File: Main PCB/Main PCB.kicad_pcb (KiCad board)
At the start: 2 copper layers, 100 x 70 mm, 43 parts, among them J1 Power Input, J10 Conn_01x03_Pin, J11 Conn_01x03_Pin, J12 Conn_01x03_Pin, J13 Conn_01x03_Pin, J14 Conn_01x03_Pin, J15 Conn_01x03_Pin, J16 Spare I2C PINS, J2 2nd PCB, J3 Servo Motor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

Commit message: Second revision
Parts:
- removed C4: C, Capacitor_THT:C_Disc_D3.8mm_W2.6mm_P2.50mm
- added C12: 10nF, Capacitor_THT:C_Disc_D3.8mm_W2.6mm_P2.50mm, F.Cu at (135.5, 128.0)
- added C13: 10uF, Capacitor_THT:C_Disc_D5.0mm_W2.5mm_P5.00mm, F.Cu at (152.8, 112.5)
- added J17: Trigger Pin (backup), Connector_PinHeader_2.54mm:PinHeader_1x01_P2.54mm_Vertical, F.Cu at (107.8, 108.5)
- added R7: 100, Resistor_THT:R_Axial_DIN0207_L6.3mm_D2.5mm_P10.16mm_Horizontal, F.Cu at (121.7, 138.0)
- C1: value 0.1uF -> 10nF; footprint Capacitor_THT:CP_Radial_D5.0mm_P2.50mm -> Capacitor_THT:C_Disc_D3.8mm_W2.6mm_P2.50mm
- C3: value 0.1uF -> 1uF
- J7: value GPS Module -> Conn_01x05_Pin; footprint Connector_PinSocket_2.54mm:PinSocket_1x04_P2.54mm_Vertical -> Connector_PinHeader_2.54mm:PinHeader_1x05_P2.54mm_Vertical
- R1: value 10.8k -> 11k
- R2: value 3.01k -> 3k
- R3: value 3.09k -> 3k
- U1: value ~ -> CA3140
- moved J7 48.0 mm to (115.5, 86.5), turned to 0 degrees
- moved R3 9.95 mm to (152.9, 131.5)
- moved C3 9.78 mm to (141.0, 126.5), turned to 0 degrees
- moved C1 9.14 mm to (123.0, 130.2)
- moved U1 6.25 mm to (149.3, 121.3), turned to 180 degrees
- moved TH1 5.56 mm to (131.2, 132.0)
- moved J6 4.85 mm to (148.9, 102.2)
- moved C9 4.72 mm to (160.5, 106.5)
- moved J16 4.13 mm to (148.9, 97.2)
- moved J4 3.74 mm to (107.8, 104.7)
- moved R5 3.58 mm to (156.8, 113.2)
- moved R1 3.54 mm to (136.9, 133.5), turned to 0 degrees
- moved C7 2.80 mm to (160.5, 100.5)
- moved R4 2.80 mm to (92.4, 88.2)
- moved J1 2.72 mm to (76.2, 90.2), turned to 0 degrees
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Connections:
- A1 pad 1: unconnected-(A1-D1/TX-Pad1) -> /D1/TX
- A1 pad 10: unconnected-(A1-D7-Pad10) -> /Trigger
- A1 pad 2: unconnected-(A1-D0/RX-Pad2) -> /D0/RX
- A1 pad 3: unconnected-(A1-~{RESET}-Pad3) -> /PC6/RESET
- A1 pad 5: unconnected-(A1-D2-Pad5) -> /D2
- A1 pad 7: unconnected-(A1-D4-Pad7) -> /D4
- C1 pad 1: +5V -> GND
- C1 pad 2: GND -> +5V
- J7 pad 1: +5V -> /D1/TX
- J7 pad 2: GND -> /D0/RX
- J7 pad 3: /SDA -> /PC6/RESET
- J7 pad 4: /SCL -> /D2
- R2 pad 1: +5V -> Net-(R2-Pad1)
- U1 pad 1: Net-(U1-+) -> unconnected-(U1-NULL-Pad1)
- U1 pad 3: +5V -> Net-(U1-+)
- U1 pad 5: /NTC_Vout(ADC3) -> unconnected-(U1-NULL-Pad5)
- U1 pad 6: (no net) -> /NTC_Vout(ADC3)
- U1 pad 7: (no net) -> +5V
- U1 pad 8: (no net) -> unconnected-(U1-STRB-Pad8)
- U2 pad 6: unconnected-(U2-INH-Pad6) -> GND
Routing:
- net +5V: track 255.1 -> 275.5 mm
- net Net-(U1-+): track 14.6 -> 31.3 mm
- net /Trigger: track 0.00 -> 13.7 mm
- net /SDA: track 36.0 -> 23.1 mm
- net /SCL: track 27.6 -> 19.9 mm
- net Net-(U1--): track 38.9 -> 31.5 mm
- net /D4: track 0.00 -> 6.54 mm
- net /D0/RX: track 0.00 -> 6.34 mm
- net /PC6/RESET: track 0.00 -> 6.34 mm
- net /D1/TX: track 0.00 -> 6.34 mm
- net /D2: track 0.00 -> 5.49 mm
- net /IN3: track 59.2 -> 63.4 mm
- net /IN1: track 68.7 -> 72.7 mm
- net /IN2: track 56.3 -> 60.2 mm
- net /IN4: track 58.0 -> 61.7 mm
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
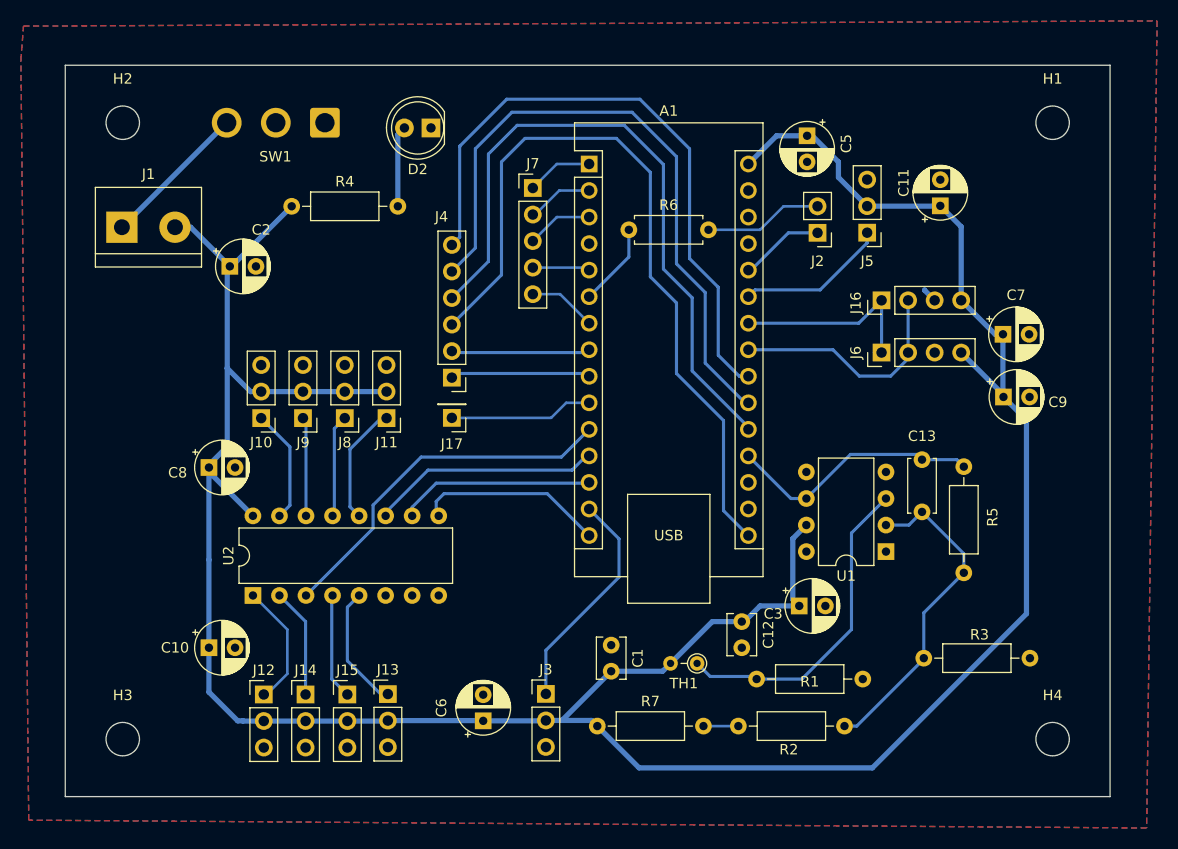
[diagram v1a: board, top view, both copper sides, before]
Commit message: Added manual vias
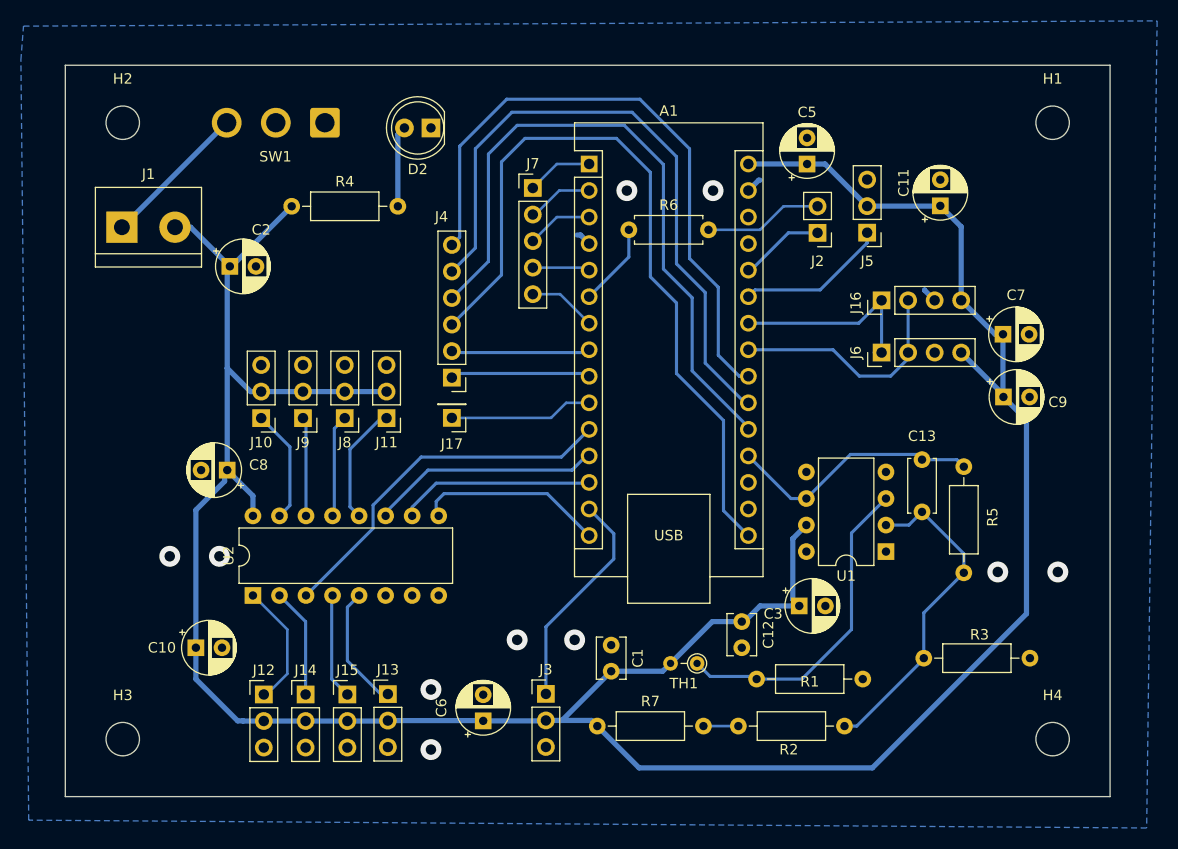
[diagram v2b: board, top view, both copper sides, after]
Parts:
- moved C5 2.71 mm to (141.8, 84.2), turned to 90 degrees
- moved C8 1.77 mm to (86.2, 113.5), turned to 180 degrees
- moved C10 1.25 mm to (83.2, 130.5)
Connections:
- A1 pad 29: unconnected-(A1-GND-Pad29) -> GND
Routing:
- net +5V: track 275.5 -> 272.1 mm
- net GND: track 1.40 -> 4.70 mm, vias 0 -> 10
- removed copper zone on F.Cu, net GND
